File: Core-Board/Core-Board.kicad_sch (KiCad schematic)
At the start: 27 parts, among them J1 POWER, J10 PCIE, J2 PCIE, J3 XT60-M, J4 PCIE, J5 PCIE, J6 ESP32-DEVKITC-32D, J7 Conn_01x19_Male, J8 PCIE, J9 Conn_01x19_Male, SW1 SW_SPST, U1 AZ1117IH-3.3TRG1, U2 74HC4050D, U3 XTSD04GLGEAG, U4 AZ1117IH-5TRG1

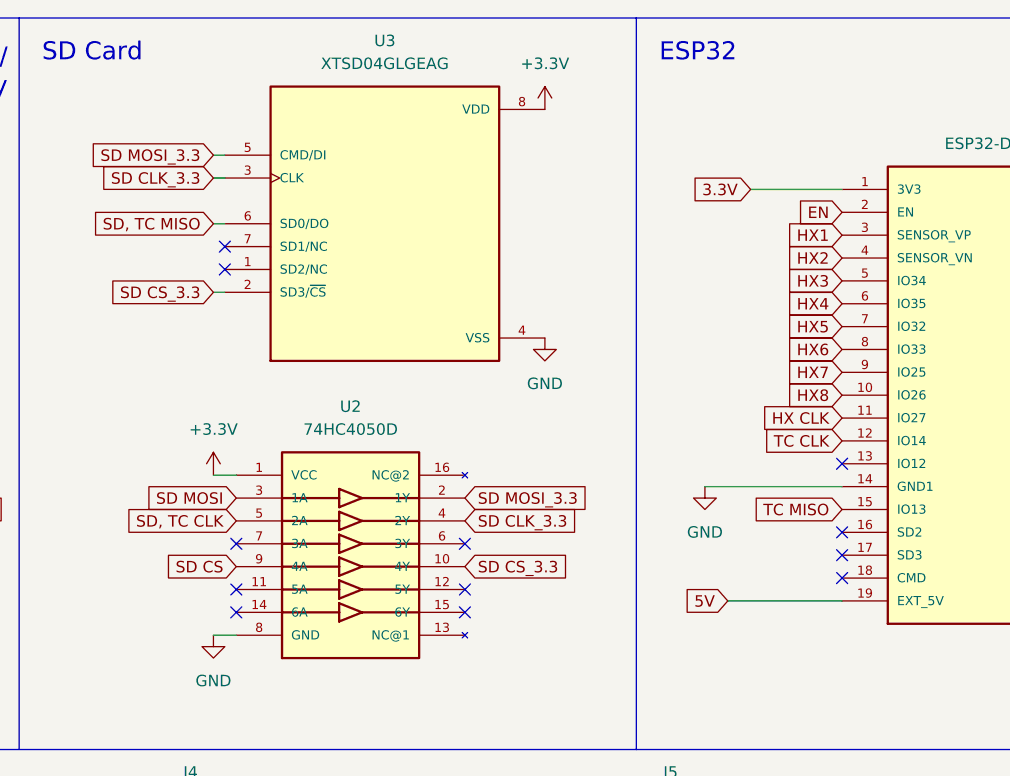
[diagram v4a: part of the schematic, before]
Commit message: Finish tracing core board. Need to do cleanup and silkscreen.
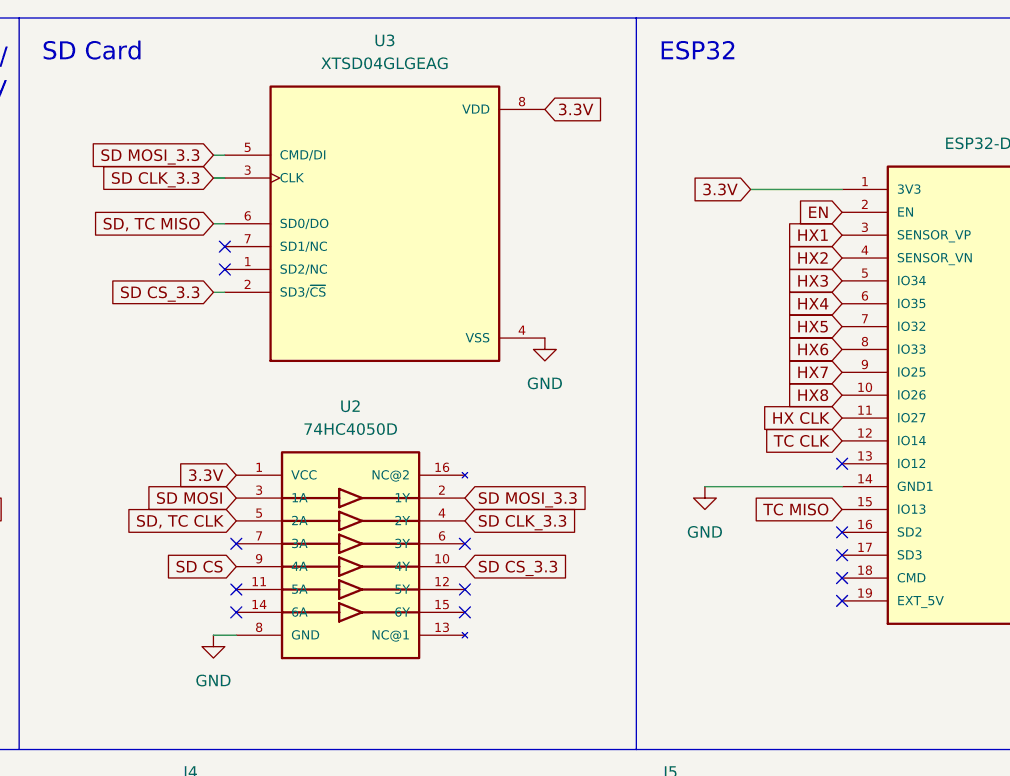
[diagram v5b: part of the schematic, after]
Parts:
- J7, J9: footprint Connector_PinHeader_1.27mm:PinHeader_1x19_P1.27mm_Vertical -> Connector_PinHeader_2.54mm:PinHeader_1x19_P2.54mm_Vertical
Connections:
- net +3.3V: no longer U2.1 (VCC), U3.8 (VDD)
- net 3.3V: now also U2.1 (VCC), U3.8 (VDD)
- net 5V: no longer J6.19 (EXT_5V)
- no-connect marks 32 -> 33
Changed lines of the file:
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@@
   (no_connect (at 256.54 132.08))
   (no_connect (at 271.78 101.6))
+  (no_connect (at 177.8 128.27))
   (no_connect (at 177.8 125.73))
   (no_connect (at 256.54 121.92))
@@
     (stroke (width 0) (type default) (color 0 0 0 0))
   )
-  (wire (pts (xy 165.1 128.27) (xy 177.8 128.27))
-    (stroke (width 0) (type default) (color 0 0 0 0))
-  )
   (wire (pts (xy 80.01 167.64) (xy 80.01 185.42))
     (stroke (width 0) (type default) (color 0 0 0 0))
@@
     (stroke (width 0) (type default) (color 0 0 0 0))
   )
-  (wire (pts (xy 107.95 114.3) (xy 110.49 114.3))
-    (stroke (width 0) (type default) (color 0 0 0 0))
-  )
   (wire (pts (xy 63.5 96.52) (xy 63.5 99.06))
     (stroke (width 0) (type default) (color 0 0 0 0))
@@
     )
   )
+  (global_label "3.3V" (shape input) (at 144.78 73.66 0) (fields_autoplaced)
+    (effects (font (size 1.27 1.27)) (justify left))
+    (property "Intersheet References" "${INTERSHEET_REFS}" (id 0) (at 151.3055 73.5806 0)
+      (effects (font (size 1.27 1.27)) (justify left) hide)
+    )
+  )
   (global_label "MOS SDA" (shape input) (at 218.44 95.25 0) (fields_autoplaced)
     (effects (font (size 1.27 1.27)) (justify left))
@@
     )
   )
-  (global_label "5V" (shape input) (at 165.1 128.27 180) (fields_autoplaced)
-    (effects (font (size 1.27 1.27)) (justify right))
-    (property "Intersheet References" "${INTERSHEET_REFS}" (id 0) (at 160.3888 128.3494 0)
-      (effects (font (size 1.27 1.27)) (justify right) hide)
-    )
-  )
   (global_label "HX8" (shape input) (at 256.54 114.3 180) (fields_autoplaced)
     (effects (font (size 1.27 1.27)) (justify right))
@@
     )
   )
+  (global_label "3.3V" (shape input) (at 110.49 114.3 180) (fields_autoplaced)
+    (effects (font (size 1.27 1.27)) (justify right))
+    (property "Intersheet References" "${INTERSHEET_REFS}" (id 0) (at 103.9645 114.3794 0)
+      (effects (font (size 1.27 1.27)) (justify right) hide)
+    )
+  )
   (global_label "SD MOSI" (shape input) (at 218.44 100.33 0) (fields_autoplaced)
     (effects (font (size 1.27 1.27)) (justify left))
@@
     (property "Reference" "J9" (id 0) (at 271.78 85.09 0))
     (property "Value" "Conn_01x19_Male" (id 1) (at 273.05 87.63 0))
-    (property "Footprint" "Connector_PinHeader_1.27mm:PinHeader_1x19_P1.27mm_Vertical" (id 2) (at 266.7 114.3 0)
+    (property "Footprint" "Connector_PinHeader_2.54mm:PinHeader_1x19_P2.54mm_Vertical" (id 2) (at 266.7 114.3 0)
       (effects (font (size 1.27 1.27)) hide)
     )
@@
     (property "Reference" "J7" (id 0) (at 260.985 142.24 0))
     (property "Value" "Conn_01x19_Male" (id 1) (at 260.985 139.7 0))
-    (property "Footprint" "Connector_PinHeader_1.27mm:PinHeader_1x19_P1.27mm_Vertical" (id 2) (at 261.62 114.3 0)
+    (property "Footprint" "Connector_PinHeader_2.54mm:PinHeader_1x19_P2.54mm_Vertical" (id 2) (at 261.62 114.3 0)
       (effects (font (size 1.27 1.27)) hide)
     )
@@
     (pin "2")
   )
-  (symbol (lib_id "power:+3.3V") (at 144.78 73.66 0) (unit 1)
-    (in_bom yes) (on_board yes) (fields_autoplaced)
-    (property "Reference" "#PWR027" (id 0) (at 144.78 77.47 0)
-      (effects (font (size 1.27 1.27)) hide)
-    )
-    (property "Value" "+3.3V" (id 1) (at 144.78 68.58 0))
-    (property "Footprint" "" (id 2) (at 144.78 73.66 0)
-      (effects (font (size 1.27 1.27)) hide)
-    )
-    (property "Datasheet" "" (id 3) (at 144.78 73.66 0)
-      (effects (font (size 1.27 1.27)) hide)
-    )
-    (pin "1")
-  )
   (symbol (lib_id "power:+5V") (at 243.84 137.16 0) (unit 1)
     (in_bom yes) (on_board yes)
@@
     (pin "1")
   )
-  (symbol (lib_id "power:+3.3V") (at 107.95 114.3 0) (unit 1)
-    (in_bom yes) (on_board yes) (fields_autoplaced)
-    (property "Reference" "#PWR019" (id 0) (at 107.95 118.11 0)
-      (effects (font (size 1.27 1.27)) hide)
-    )
-    (property "Value" "+3.3V" (id 1) (at 107.95 109.22 0))
-    (property "Footprint" "" (id 2) (at 107.95 114.3 0)
-      (effects (font (size 1.27 1.27)) hide)
-    )
-    (property "Datasheet" "" (id 3) (at 107.95 114.3 0)
-      (effects (font (size 1.27 1.27)) hide)
-    )
-    (pin "1")
-  )
   (symbol (lib_id "power:GND") (at 63.5 99.06 0) (unit 1)
     (in_bom yes) (on_board yes) (fields_autoplaced)
@@
       (reference "#PWR018") (unit 1) (value "GND") (footprint "")
     )
-    (path "/f24927b3-006b-4a5b-9480-8b7d2990d55a"
-      (reference "#PWR019") (unit 1) (value "+3.3V") (footprint "")
-    )
     (path "/6ffe48fd-1b6c-42fa-806d-65e831902546"
       (reference "#PWR020") (unit 1) (value "GND") (footprint "")
@@
       (reference "#PWR024") (unit 1) (value "+12V") (footprint "")
     )
-    (path "/683c624d-9e19-47b2-a923-3436f2000eda"
-      (reference "#PWR027") (unit 1) (value "+3.3V") (footprint "")
-    )
     (path "/486bb50a-5ff7-47f6-bf6a-ff38adfa214f"
       (reference "#PWR028") (unit 1) (value "GND") (footprint "")
@@
     )
     (path "/18bfd03e-afac-4edf-b4bb-aa290661ebea"
-      (reference "J7") (unit 1) (value "Conn_01x19_Male") (footprint "Connector_PinHeader_1.27mm:PinHeader_1x19_P1.27mm_Vertical")
+      (reference "J7") (unit 1) (value "Conn_01x19_Male") (footprint "Connector_PinHeader_2.54mm:PinHeader_1x19_P2.54mm_Vertical")
     )
     (path "/d3636d21-c771-40d8-9746-b5c1c32e4f3d"
@@
     )
     (path "/178070bc-9e77-447a-b349-b952957ba5f5"
-      (reference "J9") (unit 1) (value "Conn_01x19_Male") (footprint "Connector_PinHeader_1.27mm:PinHeader_1x19_P1.27mm_Vertical")
+      (reference "J9") (unit 1) (value "Conn_01x19_Male") (footprint "Connector_PinHeader_2.54mm:PinHeader_1x19_P2.54mm_Vertical")
     )
     (path "/54c4d0ab-46f9-43c0-898c-6a220b8fa724"

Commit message: Progress on revising ground boards.
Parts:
- added J?: DB15_Female, symbol Connector:DB15_Female
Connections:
- net 5V: now also J6.19 (EXT_5V)
- new net BAT1_+: J?.11 (P111), J?.4
- new net BAT1_-: J?.10 (P10), J?.2, J?.3
- new net BAT2_+: J?.14 (P14), J?.15 (P15), J?.7, J?.8
- new net BAT2_-: J?.12 (P12), J?.13 (P13), J?.5, J?.6
- new net Serial_RX: J?.1
- new net Serial_TX: J?.9 (P9)
- no-connect marks 33 -> 32
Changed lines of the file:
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@@
   (junction (at 186.69 185.42) (diameter 0) (color 0 0 0 0)
   )
+  (junction (at 213.614 245.872) (diameter 0) (color 0 0 0 0)
+  )
   (junction (at 240.03 185.42) (diameter 0) (color 0 0 0 0)
   )
@@
   (junction (at 367.538 114.046) (diameter 0) (color 0 0 0 0)
   )
+  (junction (at 213.614 256.032) (diameter 0) (color 0 0 0 0)
+  )
   (junction (at 80.01 167.64) (diameter 0) (color 0 0 0 0)
   )
@@
   (junction (at 92.71 200.66) (diameter 0) (color 0 0 0 0)
   )
+  (junction (at 213.614 233.172) (diameter 0) (color 0 0 0 0)
+  )
   (junction (at 92.71 190.5) (diameter 0) (color 0 0 0 0)
   )
@@
   (junction (at 133.35 185.42) (diameter 0) (color 0 0 0 0)
   )
+  (junction (at 213.614 248.412) (diameter 0) (color 0 0 0 0)
+  )
   (junction (at 39.37 200.66) (diameter 0) (color 0 0 0 0)
   )
@@
   (junction (at 74.93 193.04) (diameter 0) (color 0 0 0 0)
   )
+  (junction (at 213.614 258.572) (diameter 0) (color 0 0 0 0)
+  )
   (junction (at 278.13 200.66) (diameter 0) (color 0 0 0 0)
   )
@@
   (no_connect (at 256.54 132.08))
   (no_connect (at 271.78 101.6))
-  (no_connect (at 177.8 128.27))
   (no_connect (at 177.8 125.73))
   (no_connect (at 256.54 121.92))
@@
     (stroke (width 0) (type default) (color 0 0 0 0))
   )
+  (wire (pts (xy 213.614 258.572) (xy 213.614 261.112))
+    (stroke (width 0) (type default) (color 0 0 0 0))
+  )
   (wire (pts (xy 323.088 114.046) (xy 325.628 114.046))
     (stroke (width 0) (type default) (color 0 0 0 0))
@@
     (stroke (width 0) (type default) (color 0 0 0 0))
   )
+  (wire (pts (xy 213.614 243.332) (xy 213.614 245.872))
+    (stroke (width 0) (type default) (color 0 0 0 0))
+  )
   (wire (pts (xy 64.77 195.58) (xy 64.77 198.12))
     (stroke (width 0) (type default) (color 0 0 0 0))
@@
     (stroke (width 0) (type default) (color 0 0 0 0))
   )
+  (wire (pts (xy 213.614 245.872) (xy 213.614 248.412))
+    (stroke (width 0) (type default) (color 0 0 0 0))
+  )
   (wire (pts (xy 129.54 185.42) (xy 129.54 193.04))
     (stroke (width 0) (type default) (color 0 0 0 0))
@@
     (stroke (width 0) (type default) (color 0 0 0 0))
   )
+  (wire (pts (xy 213.614 248.412) (xy 213.614 250.952))
+    (stroke (width 0) (type default) (color 0 0 0 0))
+  )
   (wire (pts (xy 26.67 167.64) (xy 39.37 167.64))
     (stroke (width 0) (type default) (color 0 0 0 0))
@@
     (stroke (width 0) (type default) (color 0 0 0 0))
   )
+  (wire (pts (xy 213.614 256.032) (xy 213.614 258.572))
+    (stroke (width 0) (type default) (color 0 0 0 0))
+  )
   (wire (pts (xy 278.13 190.5) (xy 281.94 190.5))
     (stroke (width 0) (type default) (color 0 0 0 0))
@@
     (stroke (width 0) (type default) (color 0 0 0 0))
   )
+  (wire (pts (xy 213.614 253.492) (xy 213.614 256.032))
+    (stroke (width 0) (type default) (color 0 0 0 0))
+  )
   (wire (pts (xy 167.64 82.55) (xy 177.8 82.55))
     (stroke (width 0) (type default) (color 0 0 0 0))
@@
     (stroke (width 0) (type default) (color 0 0 0 0))
   )
+  (wire (pts (xy 213.614 238.252) (xy 213.614 240.792))
+    (stroke (width 0) (type default) (color 0 0 0 0))
+  )
   (wire (pts (xy 35.56 190.5) (xy 39.37 190.5))
     (stroke (width 0) (type default) (color 0 0 0 0))
@@
     (stroke (width 0) (type default) (color 0 0 0 0))
   )
+  (wire (pts (xy 213.614 233.172) (xy 213.614 235.712))
+    (stroke (width 0) (type default) (color 0 0 0 0))
+  )
   (wire (pts (xy 289.56 193.04) (xy 288.29 193.04))
     (stroke (width 0) (type default) (color 0 0 0 0))
@@
     (stroke (width 0) (type default) (color 0 0 0 0))
   )
+  (wire (pts (xy 213.614 230.632) (xy 213.614 233.172))
+    (stroke (width 0) (type default) (color 0 0 0 0))
+  )
   (wire (pts (xy 322.326 82.296) (xy 324.866 82.296))
     (stroke (width 0) (type default) (color 0 0 0 0))
@@
     (effects (font (size 2 2)) (justify right bottom))
   )
+  (label "Serial_TX" (at 213.614 228.092 180)
+    (effects (font (size 1.27 1.27)) (justify right bottom))
+  )
+  (label "BAT2_-" (at 213.614 243.332 180)
+    (effects (font (size 1.27 1.27)) (justify right bottom))
+  )
+  (label "BAT2_+" (at 213.614 253.492 180)
+    (effects (font (size 1.27 1.27)) (justify right bottom))
+  )
+  (label "Serial_RX" (at 213.614 225.552 180)
+    (effects (font (size 1.27 1.27)) (justify right bottom))
+  )
+  (label "BAT1_-" (at 213.614 230.632 180)
+    (effects (font (size 1.27 1.27)) (justify right bottom))
+  )
+  (label "BAT1_+" (at 213.614 238.252 180)
+    (effects (font (size 1.27 1.27)) (justify right bottom))
+  )
   (global_label "HX3" (shape input) (at 171.45 167.64 0) (fields_autoplaced)
     (effects (font (size 1.27 1.27)) (justify left))
@@
     )
   )
+  (global_label "5V" (shape input) (at 177.8 128.27 180) (fields_autoplaced)
+    (effects (font (size 1.27 1.27)) (justify right))
+    (property "Intersheet References" "${INTERSHEET_REFS}" (id 0) (at 173.0888 128.3494 0)
+      (effects (font (size 1.27 1.27)) (justify right) hide)
+    )
+  )
   (global_label "HX7" (shape input) (at 252.73 172.72 180) (fields_autoplaced)
     (effects (font (size 1.27 1.27)) (justify right))
@@
     (pin "1")
   )
+  (symbol (lib_id "Connector:DB15_Female") (at 221.234 243.332 0) (unit 1)
+    (in_bom yes) (on_board yes) (fields_autoplaced)
+    (property "Reference" "J?" (id 0) (at 225.171 242.4973 0)
+      (effects (font (size 1.27 1.27)) (justify left))
+    )
+    (property "Value" "DB15_Female" (id 1) (at 225.171 245.0342 0)
+      (effects (font (size 1.27 1.27)) (justify left))
+    )
+    (property "Footprint" "" (id 2) (at 221.234 243.332 0)
+      (effects (font (size 1.27 1.27)) hide)
+    )
+    (property "Datasheet" " ~" (id 3) (at 221.234 243.332 0)
+      (effects (font (size 1.27 1.27)) hide)
+    )
+    (pin "1")
+    (pin "10")
+    (pin "11")
+    (pin "12")
+    (pin "13")
+    (pin "14")
+    (pin "15")
+    (pin "2")
+    (pin "3")
+    (pin "4")
+    (pin "5")
+    (pin "6")
+    (pin "7")
+    (pin "8")
+    (pin "9")
+  )
   (symbol (lib_id "power:PWR_FLAG") (at 345.186 201.93 180) (unit 1)
     (in_bom yes) (on_board yes) (fields_autoplaced)
@@
       (reference "J10") (unit 1) (value "PCIE") (footprint "10018784-10210TLF:AMPHENOL_10018784-10210TLF")
     )
+    (path "/476cbb05-621c-4b08-bbf3-a0b2f1c53c15"
+      (reference "J?") (unit 1) (value "DB15_Female") (footprint "")
+    )
     (path "/fcbb5a27-40ec-4170-896c-a481825968e6"

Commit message: Further revision. Two batteries system.
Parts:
- removed F1: 6A Fuse, Fuse:Fuse_2920_7451Metric, symbol Device:Polyfuse_Small
- added C?: 22uF, Capacitor_SMD:C_0603_1608Metric, symbol Device:C_Small
- added D?: D_Small, Diode_SMD:D_0603_1608Metric, symbol Device:D_Small
- added F?: 6A Fuse, Fuse:Fuse_2920_7451Metric, symbol Device:Polyfuse_Small
- added J? (x2): Pin Jumper, symbol Connector:Conn_01x02_Male
- added J?: XT60-M, XT60-M:AMASS_XT60-M, symbol XT60-LiPO:XT60-M
- added J?: POWER, Connector:Banana_Jack_2Pin, symbol Connector:Conn_01x02_Male
- added J?: Micro_SD_Card, symbol Connector:Micro_SD_Card
- added R?: 10k, Resistor_SMD:R_0603_1608Metric, symbol Device:R_Small
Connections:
- net +12V: now also C?.2, F?.1, J?.1 (Pin_1), J?.P (POS), R?.1; no longer J1.1 (Pin_1), J3.P (POS)
- net 12V: now also F?.2; no longer F4.2
- net 3.3V: now also J?.4 (VDD)
- net BAT2_+: now also F4.2
- net BAT2_-: now also C4.1, D1.2 (A), J1.2 (Pin_2), J3.N (NEG)
- net GND: now also C?.1, D?.2 (A), J?.2 (Pin_2), J?.6 (VSS), J?.N (NEG); no longer C4.1, D1.2 (A), J1.2 (Pin_2), J3.N (NEG)
- net SD CLK_3.3: now also J?.5 (CLK)
- net SD CS_3.3: now also J?.1 (Pin_1), J?.2 (Pin_2); no longer U3.2 (SD3/~{CS})
- net SD MOSI_3.3: now also J?.3 (CMD)
- net SD, TC MISO: now also J?.7 (DAT0)
- net BAT2_+_pre: now reaches C4.2, F4.1, R1.1
- net BAT2_+_pre: now also J1.1 (Pin_1), J3.P (POS)
- new net: J?.2 (DAT3/CD), J?.2 (Pin_2)
- new net: D?.1 (K), R?.2
- new net: J?.1 (Pin_1), U3.2 (SD3/~{CS})
- no-connect marks 32 -> 35
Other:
- note added: "Battery 1: for 3v3 and 5v lines. Reference point."
- note added: "Battery 2: for high currrent/voltage needs only."
- moved on the sheet: C1, C2, C3, C4, C5, D1, F2, F3, F4, J1, J3, R1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

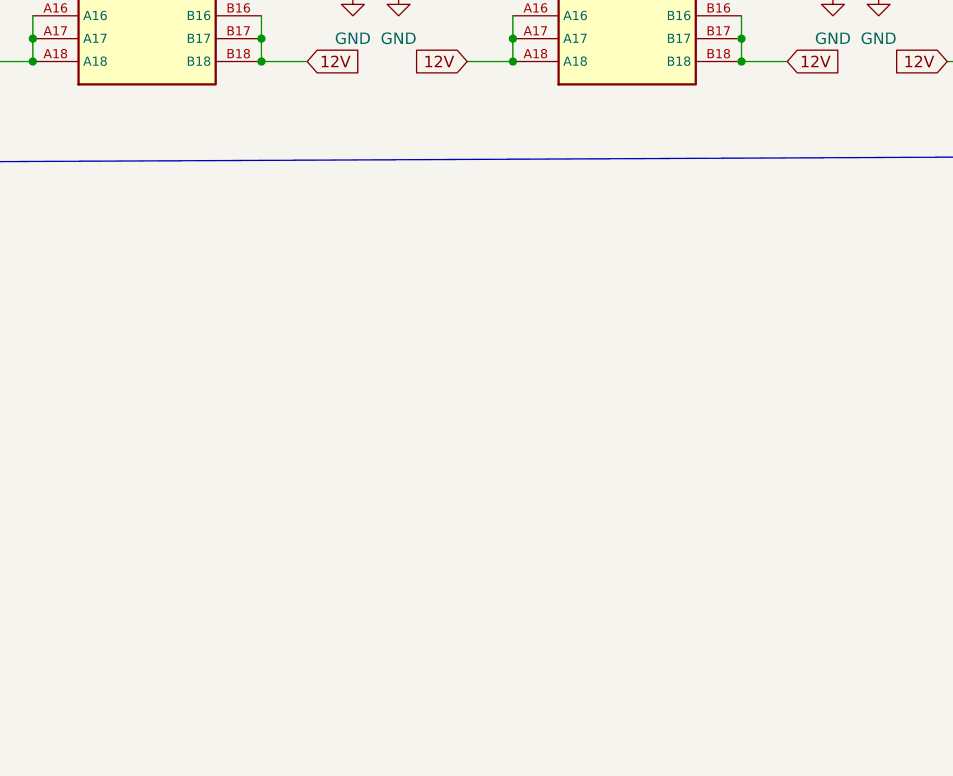
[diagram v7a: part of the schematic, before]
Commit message: Added an spi expander to core board.
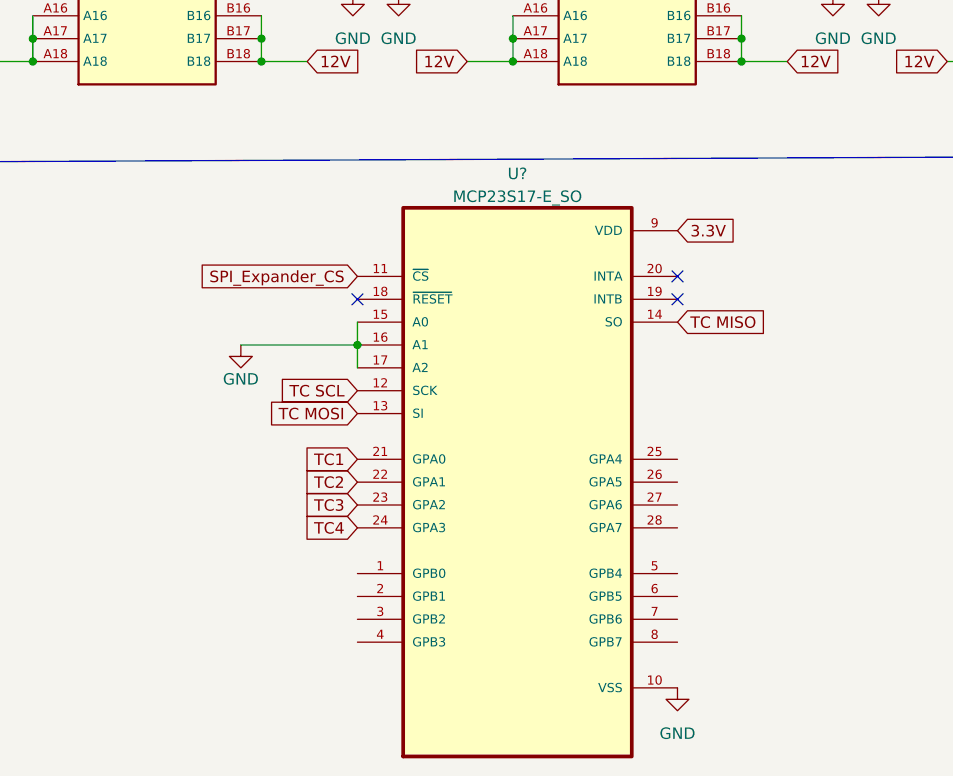
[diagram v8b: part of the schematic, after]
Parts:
- added U?: MCP23S17-E_SO, MCP23S17-E_SO:SOIC127P1030X265-28N, symbol MCP23S17-E_SO:MCP23S17-E_SO
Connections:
- net 3.3V: now also U?.9 (VDD)
- net GND: now also U?.10 (VSS), U?.15 (A0), U?.16 (A1), U?.17 (A2)
- net TC MISO: now also U?.14 (SO)
- net TC1: now also U?.21 (GPA0)
- net TC2: now also U?.22 (GPA1)
- net TC3: now also U?.23 (GPA2)
- net TC4: now also U?.24 (GPA3)
- new net SPI_Expander_CS: U?.11 (~{CS})
- new net TC MOSI: U?.13 (SI)
- new net TC SCL: U?.12 (SCK)
- no-connect marks 35 -> 38
